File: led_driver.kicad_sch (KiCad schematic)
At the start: 12 parts, among them U2 IS31FL3731-QF

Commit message: Add gerbers and assembly files
M  .gitignore
M  MyFootprints.pretty/MountingHole_2.2mm_M2_ISO7380_Pad.kicad_mod
M  MySymbols.kicad_sym
M  README.md
M  drawborder.py
A  jlcpcb/gerber/optical-keyboard-mx-B_Cu.gbl
A  jlcpcb/gerber/optical-keyboard-mx-B_Mask.gbs
A  jlcpcb/gerber/optical-keyboard-mx-B_Paste.gbp
A  jlcpcb/gerber/optical-keyboard-mx-B_Silkscreen.gbo
A  jlcpcb/gerber/optical-keyboard-mx-Edge_Cuts.gm1
A  jlcpcb/gerber/optical-keyboard-mx-F_Cu.gtl
A  jlcpcb/gerber/optical-keyboard-mx-F_Mask.gts
A  jlcpcb/gerber/optical-keyboard-mx-F_Paste.gtp
A  jlcpcb/gerber/optical-keyboard-mx-F_Silkscreen.gto
A  jlcpcb/gerber/optical-keyboard-mx-NPTH-drl_map.gbr
A  jlcpcb/gerber/optical-keyboard-mx-NPTH.drl
A  jlcpcb/gerber/optical-keyboard-mx-PTH-drl_map.gbr
A  jlcpcb/gerber/optical-keyboard-mx-PTH.drl
M  led_driver.kicad_sch
M  mounting-hw.kicad_sch
M  optical-keyboard-mx.kicad_pcb
M  optical-keyboard-mx.kicad_sch
M  placefp.py
M  switch-plate/.gitignore
A  switch-plate/jlcpcb/gerber/switch-plate-B_Cu.gbl
A  switch-plate/jlcpcb/gerber/switch-plate-B_Mask.gbs
A  switch-plate/jlcpcb/gerber/switch-plate-B_Paste.gbp
A  switch-plate/jlcpcb/gerber/switch-plate-B_Silkscreen.gbo
A  switch-plate/jlcpcb/gerber/switch-plate-Edge_Cuts.gm1
A  switch-plate/jlcpcb/gerber/switch-plate-F_Cu.gtl
A  switch-plate/jlcpcb/gerber/switch-plate-F_Mask.gts
A  switch-plate/jlcpcb/gerber/switch-plate-F_Paste.gtp
A  switch-plate/jlcpcb/gerber/switch-plate-F_Silkscreen.gto
A  switch-plate/jlcpcb/gerber/switch-plate-NPTH-drl_map.gbr
A  switch-plate/jlcpcb/gerber/switch-plate-NPTH.drl
A  switch-plate/jlcpcb/gerber/switch-plate-PTH-drl_map.gbr
A  switch-plate/jlcpcb/gerber/switch-plate-PTH.drl
M  switch-plate/switch-plate.kicad_pcb
M  switch-plate/switch-plate.kicad_prl
M  switch.kicad_sch
M  wrist-support/.gitignore
A  wrist-support/jlcpcb/gerber/wrist-support-B_Cu.gbl
A  wrist-support/jlcpcb/gerber/wrist-support-B_Mask.gbs
A  wrist-support/jlcpcb/gerber/wrist-support-B_Paste.gbp
A  wrist-support/jlcpc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
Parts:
- U2: JLCPCB (none) -> IS31FL3731-QFLS2-TR; LCSC (none) -> C191206
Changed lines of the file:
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@@
+      (effects (font (size 1.27 1.27)) hide)
+    )
+    (property "JLCPCB" "IS31FL3731-QFLS2-TR" (id 4) (at 146.05 90.17 0)
+      (effects (font (size 1.27 1.27)) hide)
+    )
+    (property "LCSC" "C191206" (id 5) (at 146.05 90.17 0)
       (effects (font (size 1.27 1.27)) hide)
     )

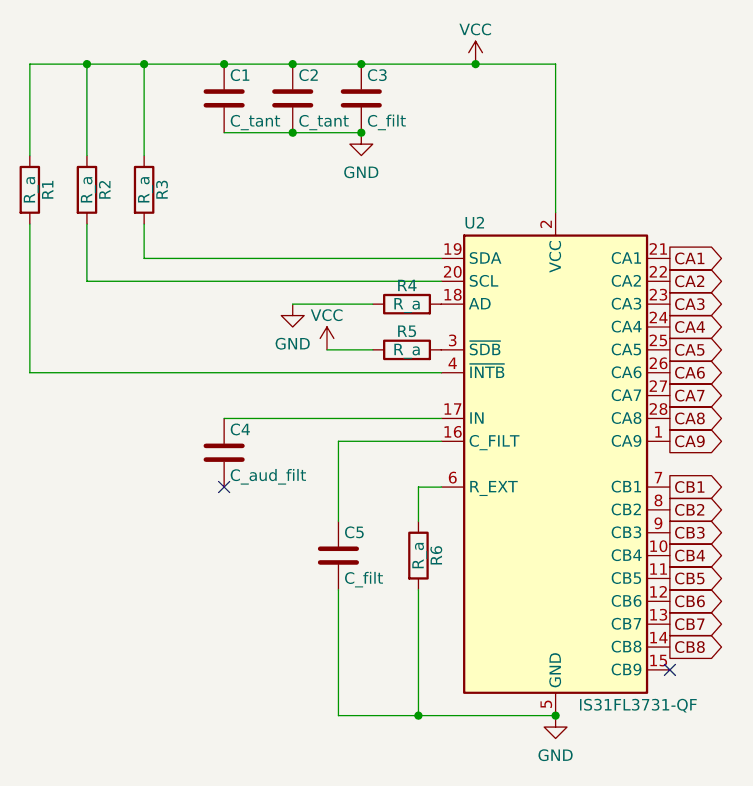
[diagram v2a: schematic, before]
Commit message: Reverse polarities of capacitor
M  jlcpcb/gerber/optical-keyboard-mx-B_Cu.gbl
M  jlcpcb/gerber/optical-keyboard-mx-B_Mask.gbs
M  jlcpcb/gerber/optical-keyboard-mx-B_Paste.gbp
M  jlcpcb/gerber/optical-keyboard-mx-B_Silkscreen.gbo
M  jlcpcb/gerber/optical-keyboard-mx-Edge_Cuts.gm1
M  jlcpcb/gerber/optical-keyboard-mx-F_Cu.gtl
M  jlcpcb/gerber/optical-keyboard-mx-F_Mask.gts
M  jlcpcb/gerber/optical-keyboard-mx-F_Paste.gtp
M  jlcpcb/gerber/optical-keyboard-mx-F_Silkscreen.gto
M  jlcpcb/gerber/optical-keyboard-mx-NPTH-drl_map.gbr
M  jlcpcb/gerber/optical-keyboard-mx-NPTH.drl
M  jlcpcb/gerber/optical-keyboard-mx-PTH-drl_map.gbr
M  jlcpcb/gerber/optical-keyboard-mx-PTH.drl
M  led_driver.kicad_sch
M  optical-keyboard-mx.kicad_pcb
M  optical-keyboard-mx.kicad_prl
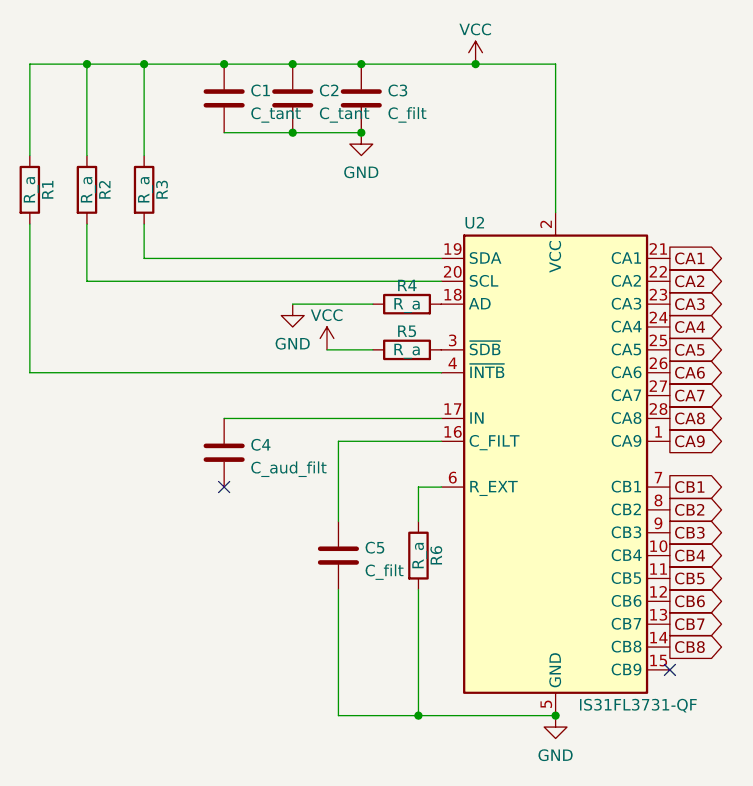
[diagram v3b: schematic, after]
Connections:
- net GND: now also C1.1, C2.1, C3.1, C5.1; no longer C1.2, C2.2, C3.2, C5.2
- net VCC: now also C1.2, C2.2, C3.2; no longer C1.1, C2.1, C3.1
- net at C4.1: no longer U2.17 (IN)
- net at C4.2: now also U2.17 (IN)
- net at U2.16 (C_FILT): now also C5.2; no longer C5.1
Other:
- moved on the sheet: C1, C2, C3, C4, C5
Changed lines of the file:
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@@
 (kicad_sch (version 20211123) (generator eeschema)
   (paper "A4")
+  (junction (at 93.98 45.72) (diameter 0) (color 0 0 0 0)
+  )
+  (junction (at 137.16 45.72) (diameter 0) (color 0 0 0 0)
+  )
+  (junction (at 146.05 118.11) (diameter 0) (color 0 0 0 0)
+  )
   (junction (at 124.46 45.72) (diameter 0) (color 0 0 0 0)
   )
-  (junction (at 93.98 45.72) (diameter 0) (color 0 0 0 0)
-  )
-  (junction (at 137.16 45.72) (diameter 0) (color 0 0 0 0)
-  )
-  (junction (at 146.05 118.11) (diameter 0) (color 0 0 0 0)
+  (junction (at 109.22 45.72) (diameter 0) (color 0 0 0 0)
   )
   (junction (at 116.84 45.72) (diameter 0) (color 0 0 0 0)
   )
-  (junction (at 109.22 45.72) (diameter 0) (color 0 0 0 0)
+  (junction (at 116.84 53.34) (diameter 0) (color 0 0 0 0)
   )
   (junction (at 100.33 45.72) (diameter 0) (color 0 0 0 0)
   )
+  (junction (at 130.81 118.11) (diameter 0) (color 0 0 0 0)
+  )
   (junction (at 124.46 53.34) (diameter 0) (color 0 0 0 0)
-  )
-  (junction (at 130.81 118.11) (diameter 0) (color 0 0 0 0)
-  )
-  (junction (at 116.84 53.34) (diameter 0) (color 0 0 0 0)
   )
   (no_connect (at 109.22 92.71))
@@
     (stroke (width 0) (type default) (color 0 0 0 0))
   )
+  (wire (pts (xy 109.22 53.34) (xy 116.84 53.34))
+    (stroke (width 0) (type default) (color 0 0 0 0))
+  )
+  (wire (pts (xy 109.22 85.09) (xy 133.35 85.09))
+    (stroke (width 0) (type default) (color 0 0 0 0))
+  )
+  (wire (pts (xy 133.35 67.31) (xy 100.33 67.31))
+    (stroke (width 0) (type default) (color 0 0 0 0))
+  )
+  (wire (pts (xy 100.33 45.72) (xy 109.22 45.72))
+    (stroke (width 0) (type default) (color 0 0 0 0))
+  )
+  (wire (pts (xy 121.92 104.14) (xy 121.92 118.11))
+    (stroke (width 0) (type default) (color 0 0 0 0))
+  )
+  (wire (pts (xy 146.05 45.72) (xy 137.16 45.72))
+    (stroke (width 0) (type default) (color 0 0 0 0))
+  )
+  (wire (pts (xy 121.92 118.11) (xy 130.81 118.11))
+    (stroke (width 0) (type default) (color 0 0 0 0))
+  )
+  (wire (pts (xy 124.46 45.72) (xy 137.16 45.72))
+    (stroke (width 0) (type default) (color 0 0 0 0))
+  )
+  (wire (pts (xy 116.84 53.34) (xy 124.46 53.34))
+    (stroke (width 0) (type default) (color 0 0 0 0))
+  )
+  (wire (pts (xy 133.35 92.71) (xy 130.81 92.71))
+    (stroke (width 0) (type default) (color 0 0 0 0))
+  )
+  (wire (pts (xy 109.22 45.72) (xy 116.84 45.72))
+    (stroke (width 0) (type default) (color 0 0 0 0))
+  )
+  (wire (pts (xy 116.84 72.39) (xy 125.73 72.39))
+    (stroke (width 0) (type default) (color 0 0 0 0))
+  )
+  (wire (pts (xy 146.05 45.72) (xy 146.05 62.23))
+    (stroke (width 0) (type default) (color 0 0 0 0))
+  )
+  (wire (pts (xy 130.81 92.71) (xy 130.81 96.52))
+    (stroke (width 0) (type default) (color 0 0 0 0))
+  )
   (wire (pts (xy 116.84 45.72) (xy 124.46 45.72))
     (stroke (width 0) (type default) (color 0 0 0 0))
   )
-  (wire (pts (xy 116.84 53.34) (xy 124.46 53.34))
-    (stroke (width 0) (type default) (color 0 0 0 0))
-  )
-  (wire (pts (xy 109.22 85.09) (xy 133.35 85.09))
-    (stroke (width 0) (type default) (color 0 0 0 0))
-  )
-  (wire (pts (xy 133.35 67.31) (xy 100.33 67.31))
-    (stroke (width 0) (type default) (color 0 0 0 0))
-  )
-  (wire (pts (xy 109.22 45.72) (xy 116.84 45.72))
-    (stroke (width 0) (type default) (color 0 0 0 0))
-  )
-  (wire (pts (xy 121.92 104.14) (xy 121.92 118.11))
-    (stroke (width 0) (type default) (color 0 0 0 0))
-  )
-  (wire (pts (xy 146.05 45.72) (xy 137.16 45.72))
-    (stroke (width 0) (type default) (color 0 0 0 0))
-  )
-  (wire (pts (xy 121.92 118.11) (xy 130.81 118.11))
-    (stroke (width 0) (type default) (color 0 0 0 0))
-  )
-  (wire (pts (xy 133.35 92.71) (xy 130.81 92.71))
-    (stroke (width 0) (type default) (color 0 0 0 0))
-  )
-  (wire (pts (xy 109.22 53.34) (xy 116.84 53.34))
-    (stroke (width 0) (type default) (color 0 0 0 0))
-  )
-  (wire (pts (xy 116.84 72.39) (xy 125.73 72.39))
-    (stroke (width 0) (type default) (color 0 0 0 0))
-  )
-  (wire (pts (xy 146.05 45.72) (xy 146.05 62.23))
-    (stroke (width 0) (type default) (color 0 0 0 0))
-  )
-  (wire (pts (xy 130.81 92.71) (xy 130.81 96.52))
-    (stroke (width 0) (type default) (color 0 0 0 0))
-  )
-  (wire (pts (xy 124.46 45.72) (xy 137.16 45.72))
-    (stroke (width 0) (type default) (color 0 0 0 0))
-  )
   (wire (pts (xy 93.98 45.72) (xy 100.33 45.72))
     (stroke (width 0) (type default) (color 0 0 0 0))
@@
     (stroke (width 0) (type default) (color 0 0 0 0))
   )
-  (wire (pts (xy 100.33 45.72) (xy 109.22 45.72))
-    (stroke (width 0) (type default) (color 0 0 0 0))
-  )
   (wire (pts (xy 100.33 67.31) (xy 100.33 63.5))
     (stroke (width 0) (type default) (color 0 0 0 0))
@@
     )
   )
-  (symbol (lib_id "MySymbols:C_tant") (at 116.84 49.53 0) (unit 1)
-    (in_bom yes) (on_board yes) (fields_autoplaced)
-    (property "Reference" "C2" (id 0) (at 117.475 46.99 0)
-      (effects (font (size 1.27 1.27)) (justify left))
-    )
-    (property "Value" "C_tant" (id 1) (at 117.475 52.07 0)
-      (effects (font (size 1.27 1.27)) (justify left))
-    )
-    (property "Footprint" "Capacitor_SMD:C_1206_3216Metric" (id 2) (at 117.8052 53.34 0)
+  (symbol (lib_id "MySymbols:C_tant") (at 116.84 49.53 180) (unit 1)
+    (in_bom yes) (on_board yes) (fields_autoplaced)
+    (property "Reference" "C2" (id 0) (at 119.761 48.6953 0)
+      (effects (font (size 1.27 1.27)) (justify right))
+    )
+    (property "Value" "C_tant" (id 1) (at 119.761 51.2322 0)
+      (effects (font (size 1.27 1.27)) (justify right))
+    )
+    (property "Footprint" "Capacitor_SMD:C_1206_3216Metric" (id 2) (at 115.8748 45.72 0)
       (effects (font (size 1.27 1.27)) hide)
     )
@@
     (pin "1")
   )
-  (symbol (lib_id "MySymbols:C_tant") (at 109.22 49.53 0) (unit 1)
-    (in_bom yes) (on_board yes) (fields_autoplaced)
-    (property "Reference" "C1" (id 0) (at 109.855 46.99 0)
-      (effects (font (size 1.27 1.27)) (justify left))
-    )
-    (property "Value" "C_tant" (id 1) (at 109.855 52.07 0)
-      (effects (font (size 1.27 1.27)) (justify left))
-    )
-    (property "Footprint" "Capacitor_SMD:C_1206_3216Metric" (id 2) (at 110.1852 53.34 0)
+  (symbol (lib_id "MySymbols:C_tant") (at 109.22 49.53 180) (unit 1)
+    (in_bom yes) (on_board yes) (fields_autoplaced)
+    (property "Reference" "C1" (id 0) (at 112.141 48.6953 0)
+      (effects (font (size 1.27 1.27)) (justify right))
+    )
+    (property "Value" "C_tant" (id 1) (at 112.141 51.2322 0)
+      (effects (font (size 1.27 1.27)) (justify right))
+    )
+    (property "Footprint" "Capacitor_SMD:C_1206_3216Metric" (id 2) (at 108.2548 45.72 0)
       (effects (font (size 1.27 1.27)) hide)
     )
@@
     (pin "1")
   )
-  (symbol (lib_id "MySymbols:C_filt") (at 124.46 49.53 0) (unit 1)
-    (in_bom yes) (on_board yes) (fields_autoplaced)
-    (property "Reference" "C3" (id 0) (at 125.095 46.99 0)
-      (effects (font (size 1.27 1.27)) (justify left))
-    )
-    (property "Value" "C_filt" (id 1) (at 125.095 52.07 0)
-      (effects (font (size 1.27 1.27)) (justify left))
-    )
-    (property "Footprint" "Capacitor_SMD:C_0603_1608Metric" (id 2) (at 125.4252 53.34 0)
+  (symbol (lib_id "MySymbols:C_filt") (at 124.46 49.53 180) (unit 1)
+    (in_bom yes) (on_board yes) (fields_autoplaced)
+    (property "Reference" "C3" (id 0) (at 127.381 48.6953 0)
+      (effects (font (size 1.27 1.27)) (justify right))
+    )
+    (property "Value" "C_filt" (id 1) (at 127.381 51.2322 0)
+      (effects (font (size 1.27 1.27)) (justify right))
+    )
+    (property "Footprint" "Capacitor_SMD:C_0603_1608Metric" (id 2) (at 123.4948 45.72 0)
       (effects (font (size 1.27 1.27)) hide)
     )
@@
     (pin "2")
   )
-  (symbol (lib_id "MySymbols:C_aud_filt") (at 109.22 88.9 0) (unit 1)
-    (in_bom yes) (on_board yes) (fields_autoplaced)
-    (property "Reference" "C4" (id 0) (at 109.855 86.36 0)
-      (effects (font (size 1.27 1.27)) (justify left))
-    )
-    (property "Value" "C_aud_filt" (id 1) (at 109.855 91.44 0)
-      (effects (font (size 1.27 1.27)) (justify left))
-    )
-    (property "Footprint" "Capacitor_SMD:C_0603_1608Metric" (id 2) (at 110.1852 92.71 0)
+  (symbol (lib_id "MySymbols:C_aud_filt") (at 109.22 88.9 180) (unit 1)
+    (in_bom yes) (on_board yes) (fields_autoplaced)
+    (property "Reference" "C4" (id 0) (at 112.141 88.0653 0)
+      (effects (font (size 1.27 1.27)) (justify right))
+    )
+    (property "Value" "C_aud_filt" (id 1) (at 112.141 90.6022 0)
+      (effects (font (size 1.27 1.27)) (justify right))
+    )
+    (property "Footprint" "Capacitor_SMD:C_0603_1608Metric" (id 2) (at 108.2548 85.09 0)
       (effects (font (size 1.27 1.27)) hide)
     )
@@
     (pin "2")
   )
-  (symbol (lib_id "MySymbols:C_filt") (at 121.92 100.33 0) (unit 1)
-    (in_bom yes) (on_board yes) (fields_autoplaced)
-    (property "Reference" "C5" (id 0) (at 122.555 97.79 0)
-      (effects (font (size 1.27 1.27)) (justify left))
-    )
-    (property "Value" "C_filt" (id 1) (at 122.555 102.87 0)
-      (effects (font (size 1.27 1.27)) (justify left))
-    )
-    (property "Footprint" "Capacitor_SMD:C_0603_1608Metric" (id 2) (at 122.8852 104.14 0)
-      (effects (font (size 1.27 1.27)) hide)
-    )
+  (symbol (lib_id "MySymbols:C_filt") (at 121.92 100.33 180) (unit 1)
+    (in_bom yes) (on_board yes) (fields_autoplaced)
+    (property "Reference" "C5" (id 0) (at 124.841 99.4953 0)
+      (effects (font (size 1.27 1.27)) (justify right))
+    )
+    (property "Value" "C_filt" (id 1) (at 124.841 102.0322 0)
+      (effects (font (size 1.27 1.27)) (justify right))
+    )
+    (property "Footprint" "Capacitor_SMD:C_0603_1608Metric" (id 2) (at 120.9548 96.52 0)
+      (effects (font (size 1.27 1.27)) hide)
+    )

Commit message: Fix bug where SCL SDA of I2c not connected
M  drawborder.py
M  led_driver.kicad_sch
M  optical-keyboard-mx.kicad_pcb
M  optical-keyboard-mx.kicad_prl
M  optical-keyboard-mx.kicad_sch
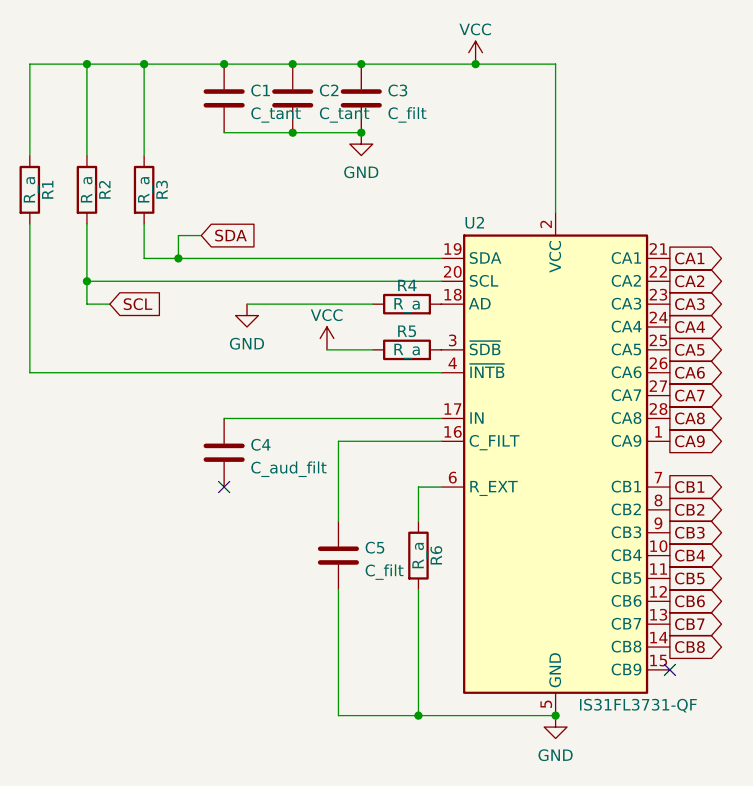
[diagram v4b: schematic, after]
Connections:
- net SDA: now reaches R3.2, U2.19 (SDA)
- net SCL: now reaches R2.2, U2.20 (SCL)
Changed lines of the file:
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@@
 (kicad_sch (version 20211123) (generator eeschema)
   (paper "A4")
+  (junction (at 93.98 69.85) (diameter 0) (color 0 0 0 0)
+  )
   (junction (at 93.98 45.72) (diameter 0) (color 0 0 0 0)
   )
@@
   )
   (junction (at 116.84 45.72) (diameter 0) (color 0 0 0 0)
+  )
+  (junction (at 104.14 67.31) (diameter 0) (color 0 0 0 0)
   )
   (junction (at 116.84 53.34) (diameter 0) (color 0 0 0 0)
@@
   (no_connect (at 109.22 92.71))
   (no_connect (at 158.75 113.03))
+  (wire (pts (xy 104.14 64.77) (xy 104.14 67.31))
+    (stroke (width 0) (type default) (color 0 0 0 0))
+  )
   (wire (pts (xy 87.63 80.01) (xy 87.63 63.5))
     (stroke (width 0) (type default) (color 0 0 0 0))
@@
     (stroke (width 0) (type default) (color 0 0 0 0))
   )
+  (wire (pts (xy 93.98 72.39) (xy 96.52 72.39))
+    (stroke (width 0) (type default) (color 0 0 0 0))
+  )
   (wire (pts (xy 93.98 69.85) (xy 93.98 63.5))
     (stroke (width 0) (type default) (color 0 0 0 0))
@@
     (stroke (width 0) (type default) (color 0 0 0 0))
   )
-  (wire (pts (xy 133.35 67.31) (xy 100.33 67.31))
+  (wire (pts (xy 133.35 67.31) (xy 104.14 67.31))
     (stroke (width 0) (type default) (color 0 0 0 0))
   )
@@
     (stroke (width 0) (type default) (color 0 0 0 0))
   )
+  (wire (pts (xy 93.98 69.85) (xy 93.98 72.39))
+    (stroke (width 0) (type default) (color 0 0 0 0))
+  )
   (wire (pts (xy 121.92 104.14) (xy 121.92 118.11))
     (stroke (width 0) (type default) (color 0 0 0 0))
@@
     (stroke (width 0) (type default) (color 0 0 0 0))
   )
-  (wire (pts (xy 116.84 72.39) (xy 125.73 72.39))
+  (wire (pts (xy 111.76 72.39) (xy 125.73 72.39))
     (stroke (width 0) (type default) (color 0 0 0 0))
   )
@@
     (stroke (width 0) (type default) (color 0 0 0 0))
   )
+  (wire (pts (xy 104.14 64.77) (xy 106.68 64.77))
+    (stroke (width 0) (type default) (color 0 0 0 0))
+  )
   (wire (pts (xy 87.63 55.88) (xy 87.63 45.72))
     (stroke (width 0) (type default) (color 0 0 0 0))
@@
     (stroke (width 0) (type default) (color 0 0 0 0))
   )
+  (wire (pts (xy 104.14 67.31) (xy 100.33 67.31))
+    (stroke (width 0) (type default) (color 0 0 0 0))
+  )
   (wire (pts (xy 100.33 67.31) (xy 100.33 63.5))
     (stroke (width 0) (type default) (color 0 0 0 0))
@@
     )
   )
+  (global_label "SDA" (shape input) (at 106.68 64.77 0) (fields_autoplaced)
+    (effects (font (size 1.27 1.27)) (justify left))
+    (property "Intersheet References" "${INTERSHEET_REFS}" (id 0) (at 112.6612 64.6906 0)
+      (effects (font (size 1.27 1.27)) (justify left) hide)
+    )
+  )
   (global_label "CB8" (shape output) (at 158.75 110.49 0) (fields_autoplaced)
     (effects (font (size 1.27 1.27)) (justify left))
     (property "Intersheet References" "${INTERSHEET_REFS}" (id 0) (at 164.9126 110.4106 0)
+      (effects (font (size 1.27 1.27)) (justify left) hide)
+    )
+  )
+  (global_label "SCL" (shape input) (at 96.52 72.39 0) (fields_autoplaced)
+    (effects (font (size 1.27 1.27)) (justify left))
+    (property "Intersheet References" "${INTERSHEET_REFS}" (id 0) (at 102.4407 72.3106 0)
       (effects (font (size 1.27 1.27)) (justify left) hide)
     )
@@
     (pin "2")
   )
-  (symbol (lib_id "power:GND") (at 116.84 72.39 0) (unit 1)
-    (in_bom yes) (on_board yes) (fields_autoplaced)
-    (property "Reference" "#PWR091" (id 0) (at 116.84 78.74 0)
-      (effects (font (size 1.27 1.27)) hide)
-    )
-    (property "Value" "GND" (id 1) (at 116.84 76.8334 0))
-    (property "Footprint" "" (id 2) (at 116.84 72.39 0)
-      (effects (font (size 1.27 1.27)) hide)
-    )
-    (property "Datasheet" "" (id 3) (at 116.84 72.39 0)
-      (effects (font (size 1.27 1.27)) hide)
-    )
+  (symbol (lib_id "power:GND") (at 111.76 72.39 0) (unit 1)
+    (in_bom yes) (on_board yes) (fields_autoplaced)
+    (property "Reference" "#PWR091" (id 0) (at 111.76 78.74 0)
+      (effects (font (size 1.27 1.27)) hide)
+    )
+    (property "Value" "GND" (id 1) (at 111.76 76.8334 0))
+    (property "Footprint" "" (id 2) (at 111.76 72.39 0)
+      (effects (font (size 1.27 1.27)) hide)
+    )
+    (property "Datasheet" "" (id 3) (at 111.76 72.39 0)
+      (effects (font (size 1.27 1.27)) hide)
+    )
